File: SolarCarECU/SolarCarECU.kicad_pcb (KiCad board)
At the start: 2 copper layers, 160 x 100.3 mm, 104 parts, among them J1 Screw_Terminal_01x02, J2 USB_B_Micro, J3 Screw_Terminal_01x04, J4 Screw_Terminal_01x08, J5 Screw_Terminal_01x08, J6 Screw_Terminal_01x14, J7 Screw_Terminal_01x14, Q1 QM6015D, Q2 PZT2222A, Q3 QM6015D, Q4 QM6015D, Q5 QM6015D, Q6 QM6015D, U1 Teensy3.6, U10 LM324A, U2 EL7202CN, U3 EL7202CN, U4 L7805, U5 MCP2562-E-P, U6 MCP2562-E-P, U7 4504, U8 4504, U9 4504

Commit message: begun layout of PCB
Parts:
- moved R9 205.6 mm to (237.5, 119.4)
- moved D1 195.0 mm to (224.8, 92.7)
- moved U6 185.0 mm to (226.1, 119.4)
- moved R41 182.4 mm to (190.5, 39.4)
- moved R32 180.6 mm to (182.9, 35.6)
- moved R1 179.1 mm to (171.4, 20.3)
- moved R40 172.8 mm to (186.7, 39.4)
- moved U10 172.7 mm to (208.3, 30.5)
- moved R39 172.5 mm to (182.9, 39.4)
- moved R24 168.9 mm to (179.1, 31.8)
- moved R16 167.1 mm to (175.3, 27.9)
- moved R17 166.9 mm to (179.1, 27.9)
- moved J6 166.3 mm to (241.6, 81.3)
- moved R21 162.6 mm to (194.3, 27.9)
- moved R38 162.2 mm to (179.1, 39.4)
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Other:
- board size 160 x 100.3 mm -> 160 x 100 mm

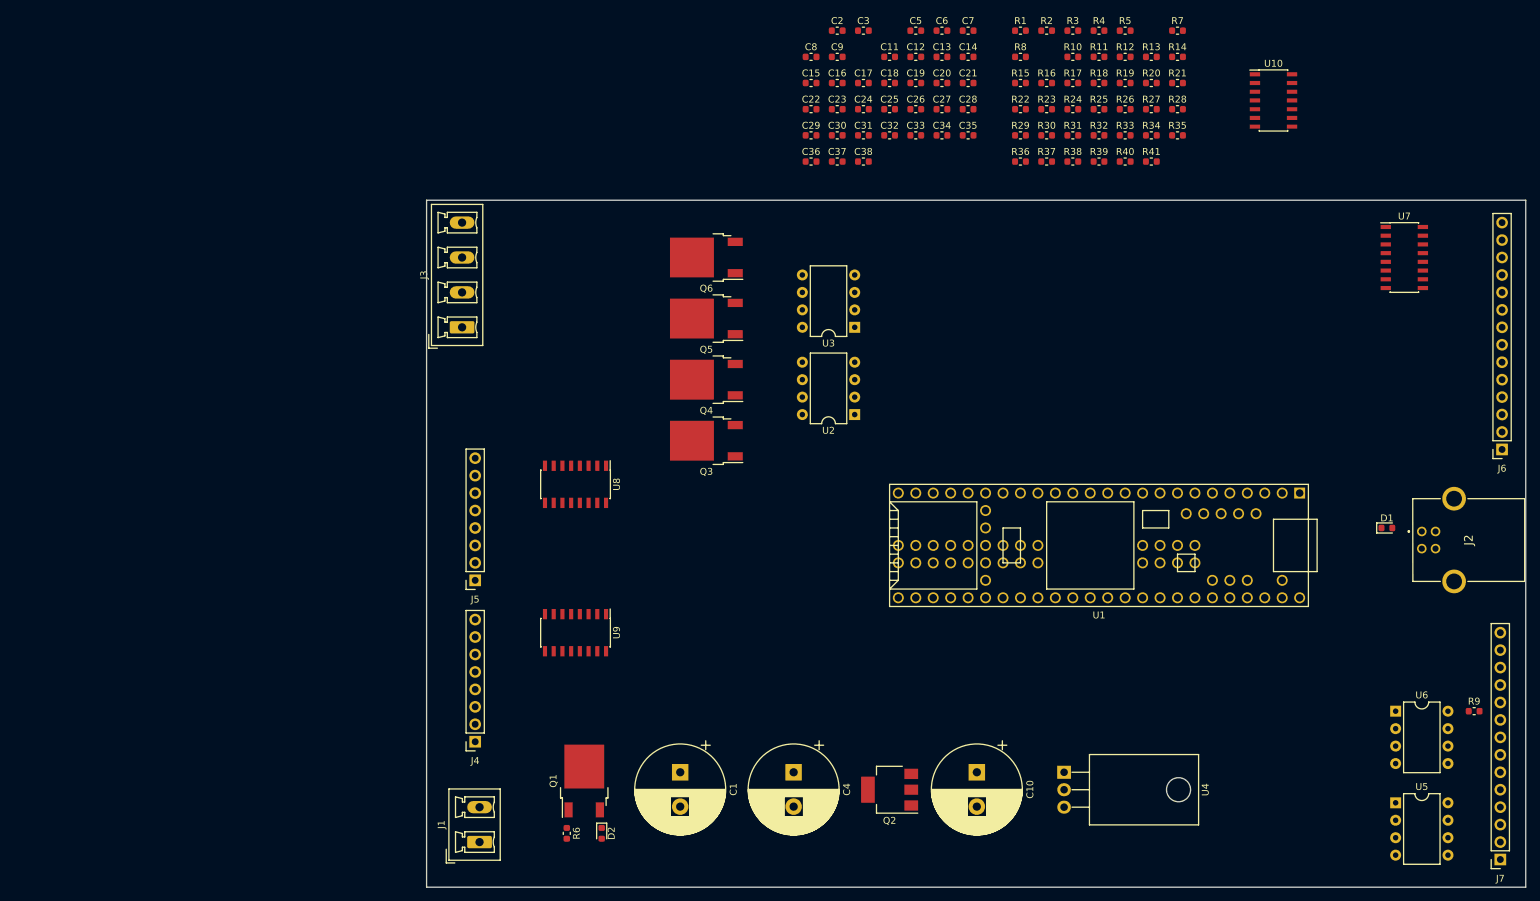
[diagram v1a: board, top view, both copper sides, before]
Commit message: Component Layout MC
MOSFET Driver, Level Shifter, OpAmp
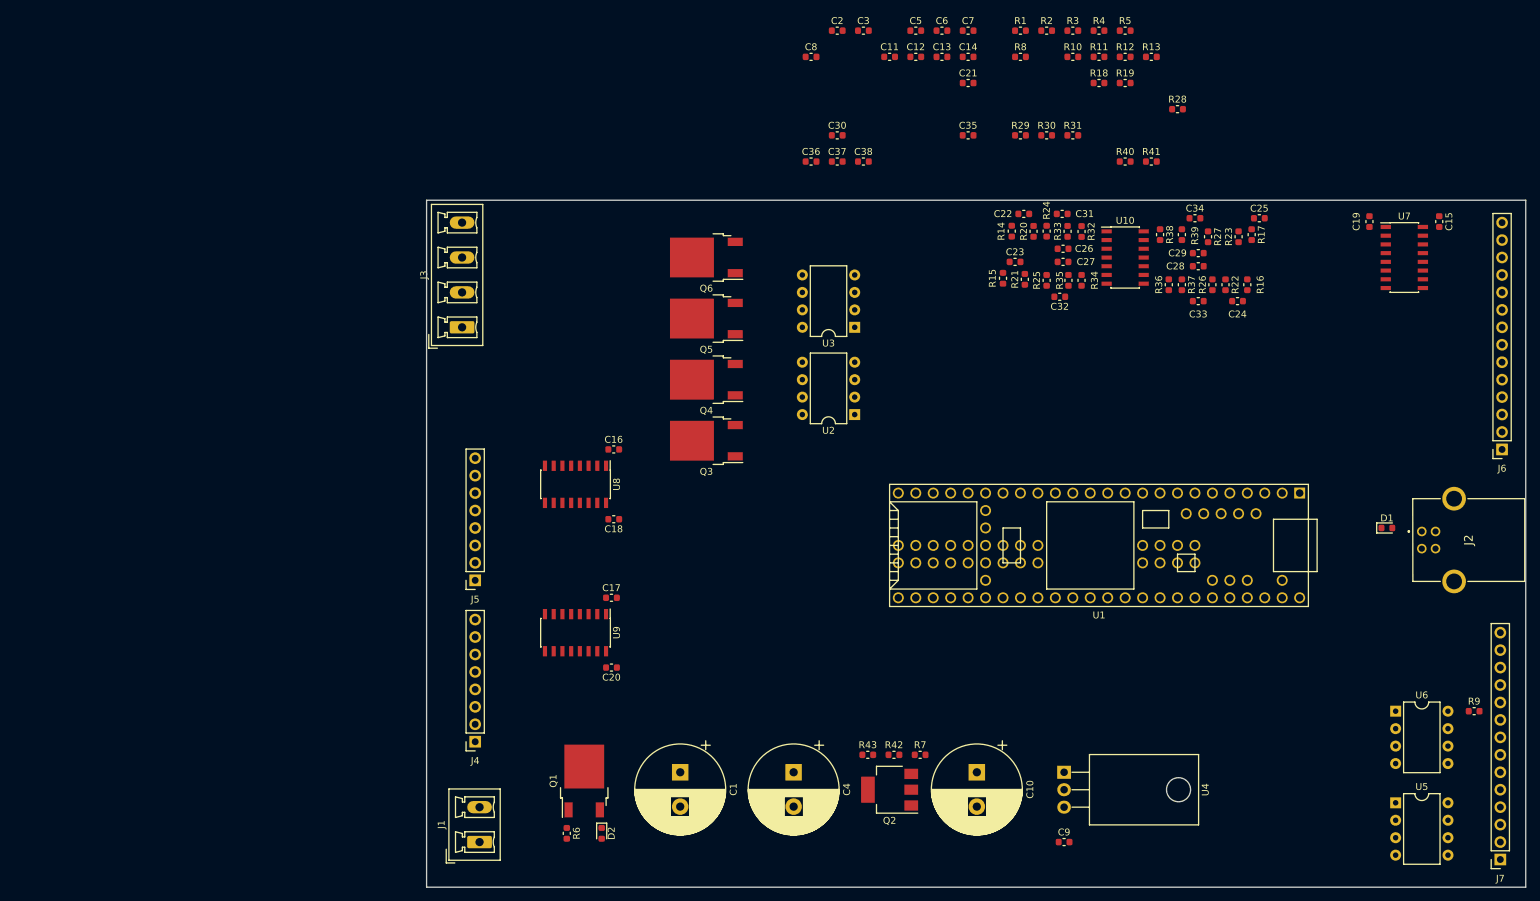
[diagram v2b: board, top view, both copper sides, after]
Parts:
- added R42: R, Resistor_SMD:R_0603_1608Metric, F.Cu at (153.0, 125.7)
- added R43: R, Resistor_SMD:R_0603_1608Metric, F.Cu at (149.2, 125.7)
- moved C9 119.0 mm to (177.8, 138.4)
- moved R7 111.9 mm to (156.8, 125.7)
- moved C20 97.7 mm to (111.9, 113.0), turned to 180 degrees
- moved C15 93.6 mm to (232.4, 48.1), turned to 270 degrees
- moved C17 83.4 mm to (111.9, 102.9)
- moved C18 75.1 mm to (112.2, 91.4), turned to 180 degrees
- moved C19 69.1 mm to (222.2, 48.1), turned to 270 degrees
- moved C16 62.5 mm to (112.2, 81.3)
- moved C24 61.2 mm to (203.0, 59.7)
- moved C29 58.9 mm to (197.3, 52.7), turned to 180 degrees
- moved C25 56.1 mm to (206.2, 47.6)
- moved C33 47.7 mm to (197.3, 59.7)
- moved R16 41.4 mm to (204.5, 57.3), turned to 90 degrees
- moved C28 40.6 mm to (197.3, 54.6), turned to 180 degrees
- moved R22 39.3 mm to (201.3, 57.3), turned to 270 degrees
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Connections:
- C1 pad 1: +12V -> Net-(C1-Pad1)
- D2 pad 1: +12V -> Net-(C1-Pad1)
- Q1 pad 3: +12V -> Net-(C1-Pad1)
- Q2 pad 2: +12V -> Net-(C1-Pad1)
- R7 pad 1: +12V -> Net-(C1-Pad1)

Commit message: Motor controller Routing
GND Vias not completed.
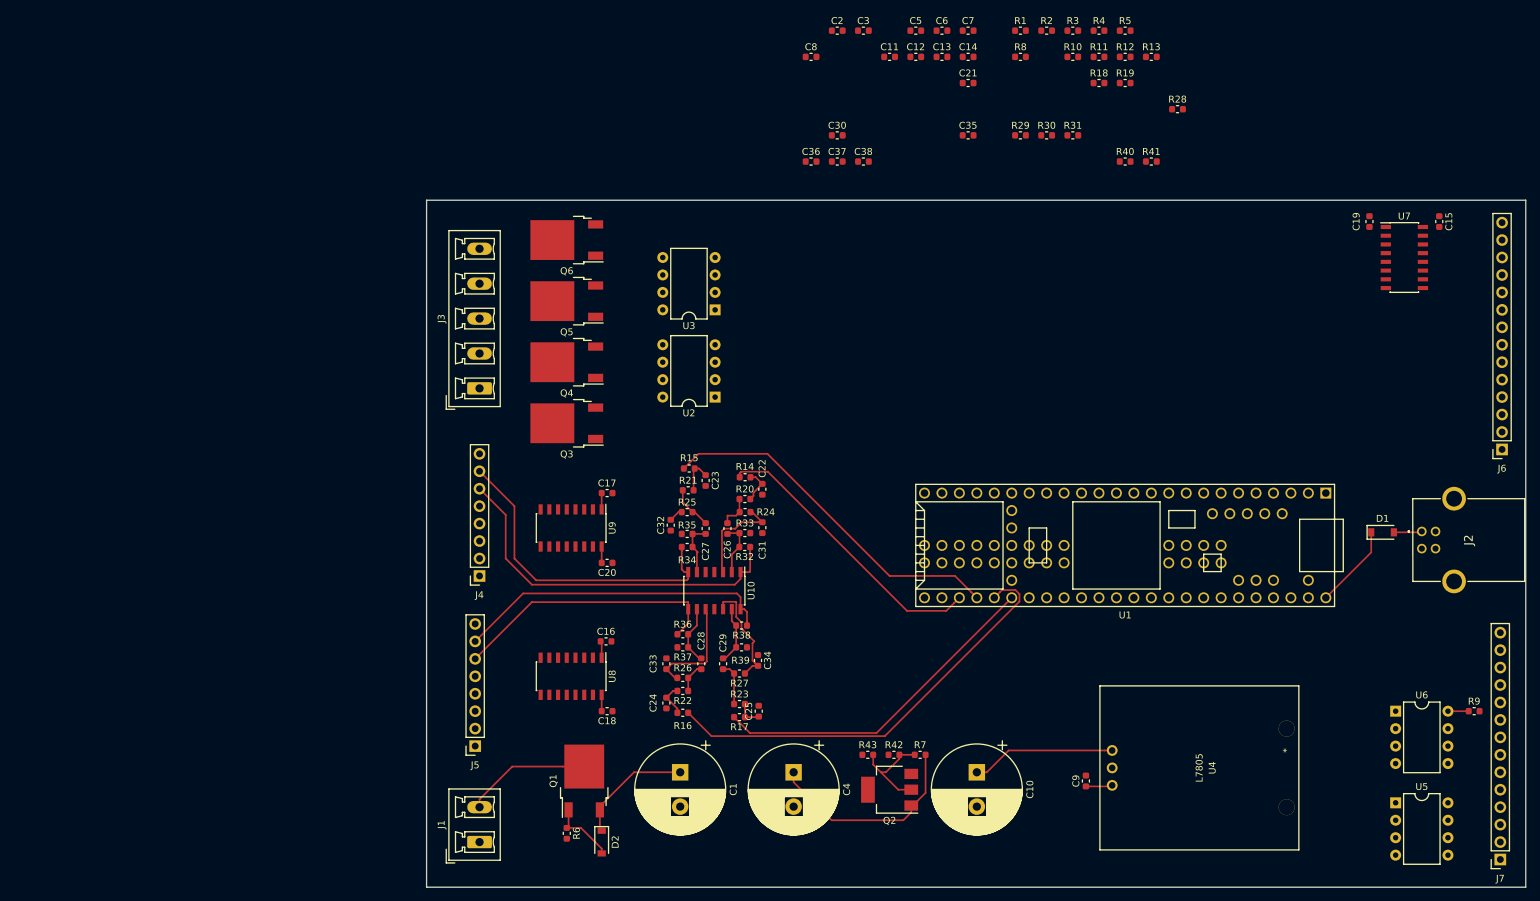
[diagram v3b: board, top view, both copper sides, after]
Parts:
- D1, D2: footprint Diode_SMD:D_0603_1608Metric -> Diode_SMD:D_SOD-123
- J3: value Screw_Terminal_01x04 -> Screw_Terminal_01x05; footprint Connector_Phoenix_MC_HighVoltage:PhoenixContact_MCV_1,5_4-G-5.08_1x04_P5.08mm_Vertical -> Connector_Phoenix_MC_HighVoltage:PhoenixContact_MCV_1,5_5-G-5.08_1x05_P5.08mm_Vertical
- U4: footprint Package_TO_SOT_THT:TO-220-3_Horizontal_TabDown -> PCBDesign:PT78NR112H
- moved R16 103.1 mm to (122.3, 119.6), turned to 0 degrees
- moved R17 102.4 mm to (130.6, 120.2), turned to 180 degrees
- moved C25 102.3 mm to (133.3, 119.4), turned to 90 degrees
- moved C24 101.7 mm to (119.9, 118.2), turned to 270 degrees
- moved R23 99.5 mm to (130.6, 118.3), turned to 0 degrees
- moved R22 98.7 mm to (122.3, 116.4), turned to 180 degrees
- moved R26 96.0 mm to (122.3, 114.5), turned to 0 degrees
- moved C33 93.7 mm to (119.9, 112.5), turned to 270 degrees
- moved R27 93.2 mm to (130.6, 113.9), turned to 180 degrees
- moved C28 92.6 mm to (125.0, 112.5), turned to 90 degrees
- moved C29 91.4 mm to (128.2, 112.5), turned to 90 degrees
- moved C34 90.5 mm to (133.2, 112.0), turned to 270 degrees
- moved R37 89.8 mm to (122.3, 110.1), turned to 180 degrees
- moved R39 87.8 mm to (130.9, 110.1), turned to 0 degrees
- moved R36 87.1 mm to (122.3, 108.2), turned to 0 degrees
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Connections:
- J3 pad 1: /HEADLIGHTS -> /HORN
- J3 pad 2: /BRAKELIGHTS -> /HEADLIGHTS
- J3 pad 3: /BLINKERS -> /BRAKELIGHTS
- J3 pad 4: GND -> /BLINKERS
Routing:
- net /PWM_MOTOR_R_THROTTLE: track 0.00 -> 63.2 mm
- net /MOTOR_L_THROTTLE: track 0.00 -> 53.8 mm
- net /PWM_MOTOR_L_REGEN: track 0.00 -> 52.2 mm
- net /PWM_MOTOR_R_REGEN: track 0.00 -> 49.5 mm
- net /MOTOR_L_REGEN: track 0.00 -> 46.9 mm
- net /MOTOR_R_REGEN: track 0.00 -> 46.6 mm
- net /PWM_MOTOR_L_THROTTLE: track 0.00 -> 41.8 mm
- net /MOTOR_R_THROTTLE: track 0.00 -> 39.7 mm
- net +5V: track 0.00 -> 33.3 mm
- net Net-(C1-Pad1): track 0.00 -> 32.2 mm
- net Net-(C4-Pad1): track 0.00 -> 30.7 mm
- net Net-(J1-Pad2): track 0.00 -> 18.4 mm
- net Net-(C33-Pad2): track 0.00 -> 16.1 mm
- net Net-(C34-Pad2): track 0.00 -> 16.1 mm
- net Net-(C31-Pad2): track 0.00 -> 15.7 mm
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
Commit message: MC Routing
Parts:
- added C39: C, Capacitor_SMD:C_0603_1608Metric, F.Cu at (152.2, 39.4)
- added C40: C, Capacitor_SMD:C_0603_1608Metric, F.Cu at (156.1, 39.4)
- added R44: R, Resistor_SMD:R_0603_1608Metric, F.Cu at (171.3, 38.7)
- added R45: R, Resistor_SMD:R_0603_1608Metric, F.Cu at (175.1, 38.7)
- added R46: R, Resistor_SMD:R_0603_1608Metric, F.Cu at (178.9, 38.7)
- added R47: R, Resistor_SMD:R_0603_1608Metric, F.Cu at (182.7, 38.7)
- moved C36 59.0 mm to (127.0, 96.7), turned to 270 degrees
- moved Q4 8.89 mm to (105.6, 59.7)
- moved Q5 8.89 mm to (105.4, 68.6)
- moved R40 3.81 mm to (186.7, 35.6)
- moved R41 3.81 mm to (190.5, 35.6)
- moved C16 1.28 mm to (111.3, 108.0)
- moved R6 0.83 mm to (105.7, 137.9)
- moved D2 0.37 mm to (110.2, 138.2)
- turned C15 to 90 degrees
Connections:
- J4 pad 1: /MOTOR_L_REV_EN -> /MOTOR_R_REGEN
- J4 pad 2: /MOTOR_L_FWD_EN -> /MOTOR_L_THROTTLE
- J4 pad 3: /MOTOR_L_REGEN_EN -> /MOTOR_L_REGEN
- J4 pad 4: /MOTOR_L_ECO_EN -> /MOTOR_L_FWD_EN
- J4 pad 5: /MOTOR_L_METER -> /MOTOR_L_REV_EN
- J4 pad 6: /MOTOR_L_THROTTLE -> /MOTOR_L_METER
- J4 pad 7: /MOTOR_L_REGEN -> /MOTOR_R_METER
- J5 pad 1: /MOTOR_R_REV_EN -> /MOTOR_R_ECO_EN
- J5 pad 2: /MOTOR_R_FWD_EN -> /MOTOR_R_REGEN_EN
- J5 pad 3: /MOTOR_R_REGEN_EN -> /MOTOR_R_FWD_EN
- J5 pad 4: /MOTOR_R_ECO_EN -> /MOTOR_L_REGEN_EN
- J5 pad 5: /MOTOR_R_METER -> /MOTOR_L_ECO_EN
- J5 pad 6: /MOTOR_R_THROTTLE -> /MOTOR_R_REV_EN
- J5 pad 7: /MOTOR_R_REGEN -> /MOTOR_R_THROTTLE
- U1 pad 34: /PWM_MOTOR_R_THROTTLE -> /PWM_MOTOR_R_REGEN
- U1 pad 35: /PWM_MOTOR_R_REGEN -> /PWM_MOTOR_R_THROTTLE
- U1 pad 36: Net-(U1-Pad36) -> /LV_MOTOR_R_ECO_EN
- U1 pad 56: Net-(U1-Pad56) -> /LV_MOTOR_R_METER
- U1 pad 57: Net-(U1-Pad57) -> /LV_MOTOR_L_METER
- U1 pad 69: Net-(U1-Pad69) -> /LV_MOTOR_L_FWD_EN
- U1 pad 78: Net-(U1-Pad78) -> /LV_MOTOR_L_ECO_EN
- U1 pad 79: Net-(U1-Pad79) -> /LV_MOTOR_L_REGEN_EN
- U1 pad 80: Net-(U1-Pad80) -> /LV_MOTOR_R_REV_EN
- U1 pad 81: Net-(U1-Pad81) -> /LV_MOTOR_R_FWD_EN
- U1 pad 82: Net-(U1-Pad82) -> /LV_MOTOR_R_REGEN_EN
- U1 pad 83: Net-(U1-Pad83) -> /LV_MOTOR_L_REV_EN
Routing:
- net GNDA: track 0.00 -> 275.4 mm, vias 0 -> 10
- net /LV_MOTOR_R_REGEN_EN: track 0.00 -> 111.7 mm, vias 0 -> 1
- net /LV_MOTOR_R_FWD_EN: track 0.00 -> 108.9 mm, vias 0 -> 1
- net /LV_MOTOR_R_ECO_EN: track 0.00 -> 108.8 mm, vias 0 -> 1
- net /LV_MOTOR_L_REV_EN: track 0.00 -> 102.4 mm, vias 0 -> 1
- net /LV_MOTOR_R_REV_EN: track 0.00 -> 95.5 mm, vias 0 -> 1
- net /LV_MOTOR_L_REGEN_EN: track 0.00 -> 88.7 mm, vias 0 -> 1
- net /LV_MOTOR_L_ECO_EN: track 0.00 -> 87.0 mm, vias 0 -> 1
- net /LV_MOTOR_L_FWD_EN: track 0.00 -> 77.7 mm, vias 0 -> 1
- net GND: track 0.00 -> 39.5 mm, vias 0 -> 16
- net /MOTOR_L_FWD_EN: track 0.00 -> 21.2 mm
- net /MOTOR_R_ECO_EN: track 0.00 -> 20.5 mm
- net /MOTOR_L_REGEN_EN: track 0.00 -> 19.6 mm
- net /MOTOR_L_REV_EN: track 0.00 -> 16.8 mm
- net /MOTOR_L_ECO_EN: track 0.00 -> 16.0 mm
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- added copper zone on In1.Cu, net +3V3
- added copper zone on In2.Cu, net GND
- added copper zone on B.Cu, net GNDA
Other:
- copper layers 2 -> 4

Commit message: lots of things
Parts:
- added R48: 4.7, Resistor_SMD:R_0603_1608Metric, F.Cu at (194.4, 70.5)
- added R49: 4.7, Resistor_SMD:R_0603_1608Metric, F.Cu at (197.5, 70.5)
- added R50: 4.7, Resistor_SMD:R_0603_1608Metric, F.Cu at (200.5, 70.5)
- added R51: 4.7, Resistor_SMD:R_0603_1608Metric, F.Cu at (116.7, 52.8)
- R32, R33, R34, R35, R36, R37, R38, R39, R6: value R -> 1k
- R42, R43: value R -> 0
- R8, R9: value R -> 100k
- moved C14 137.4 mm to (236.2, 141.0)
- moved C11 133.3 mm to (224.2, 136.5), turned to 90 degrees
- moved C13 130.6 mm to (236.2, 130.2)
- moved R2 127.9 mm to (222.9, 139.1), turned to 180 degrees
- moved R4 127.1 mm to (222.9, 141.0), turned to 180 degrees
- moved R8 127.0 mm to (236.2, 133.3)
- moved R11 125.8 mm to (238.1, 137.2), turned to 270 degrees
- moved R1 122.5 mm to (222.9, 131.4), turned to 180 degrees
- moved C12 121.5 mm to (224.0, 125.0), turned to 90 degrees
- moved R3 121.2 mm to (222.9, 133.3), turned to 180 degrees
- moved R10 116.3 mm to (235.6, 125.7), turned to 270 degrees
- moved R5 76.7 mm to (221.0, 88.9), turned to 180 degrees
- moved C2 68.2 mm to (204.5, 53.3)
- moved C30 64.9 mm to (204.5, 61.0)
- moved C37 64.9 mm to (204.5, 64.8)
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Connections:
- C2 pad 2: Net-(C2-Pad2) -> +12V
- C3 pad 2: Net-(C3-Pad2) -> +12V
- C5 pad 2: Net-(C2-Pad2) -> +12V
- C6 pad 2: Net-(C3-Pad2) -> +12V
- C7 pad 2: Net-(C2-Pad2) -> +12V
- C8 pad 2: Net-(C3-Pad2) -> +12V
- J6 pad 10: /HAZARD_LED -> /DOWN_CTRL
- J6 pad 11: /DOWN_CTRL -> /UP_CTRL
- J6 pad 12: /UP_CTRL -> /SEL_CTRL
- J6 pad 13: /SEL_CTRL -> /KILL_SENSE
- J6 pad 14: /KILL_SENSE -> /HAZARD_LED
- J7 pad 2: CAN0_H -> /CAN0_L
- J7 pad 3: CAN0_L -> /CAN0_H
- J7 pad 4: CAN1_H -> /CAN1_L
- J7 pad 5: CAN1_L -> /CAN1_H
- Q3 pad 3: Net-(C2-Pad2) -> +12V
- Q4 pad 3: Net-(C3-Pad2) -> +12V
- Q5 pad 3: Net-(C2-Pad2) -> +12V
- Q6 pad 3: Net-(C3-Pad2) -> +12V
- R10 pad 1: CAN1_H -> /CAN1_H
- R10 pad 2: CAN1_L -> /CAN1_L
- R11 pad 1: CAN0_H -> /CAN0_H
- R11 pad 2: CAN0_L -> /CAN0_L
- U2 pad 5: Net-(Q5-Pad1) -> Net-(R49-Pad2)
- U2 pad 6: Net-(C2-Pad2) -> +12V
- U2 pad 7: Net-(Q3-Pad1) -> Net-(R48-Pad2)
- U3 pad 5: Net-(Q6-Pad1) -> Net-(R51-Pad2)
- U3 pad 6: Net-(C3-Pad2) -> +12V
- U3 pad 7: Net-(Q4-Pad1) -> Net-(R50-Pad2)
- U5 pad 6: CAN0_L -> /CAN0_L
- U5 pad 7: CAN0_H -> /CAN0_H
- U6 pad 6: CAN1_L -> /CAN1_L
- U6 pad 7: CAN1_H -> /CAN1_H
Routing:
- net /LV_HEADLIGHTS: track 0.00 -> 97.4 mm
- net /CAN1_RX: track 0.00 -> 90.6 mm, vias 0 -> 1
- net Net-(R4-Pad2): track 0.00 -> 90.4 mm
- net /LV_HORN: track 0.00 -> 87.6 mm
- net Net-(R3-Pad2): track 0.00 -> 84.7 mm
- net /CAN1_TX: track 0.00 -> 84.5 mm, vias 0 -> 1
- net /LV_BRAKELIGHTS: track 0.00 -> 83.4 mm, vias 0 -> 2
- net Net-(R2-Pad2): track 0.00 -> 60.3 mm
- net Net-(R1-Pad2): track 0.00 -> 50.6 mm
- net Net-(C9-Pad1): track 3.89 -> 38.0 mm, vias 0 -> 1
- net Net-(C1-Pad1): track 31.8 -> 64.1 mm
- net /USB_D+: track 0.00 -> 29.5 mm, vias 0 -> 1
- net /USB_D-: track 0.00 -> 25.0 mm, vias 0 -> 1
- net GNDA: track 275.4 -> 290.1 mm
- net /BLINKERS: track 0.00 -> 13.2 mm
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- added copper zone on F.Cu, net +12V
